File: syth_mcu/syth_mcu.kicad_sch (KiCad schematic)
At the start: 25 parts, among them J1 Conn_01x05, J10 Conn_01x20, J11 Conn_01x20, J2 Conn_01x05, J5 Conn_01x20, J6 Conn_01x20, J7 Conn_01x16, J8 Conn_01x08, SW1 SW_Push, SW2 SW_Push, SW3 SW_Push, SW4 SW_Push, SW5 SW_Push, SW6 SW_Push, SW7 SW_SPST, U2 YAAJ_WeAct_BlackPill_Part_Like, U5 TFT_320x240

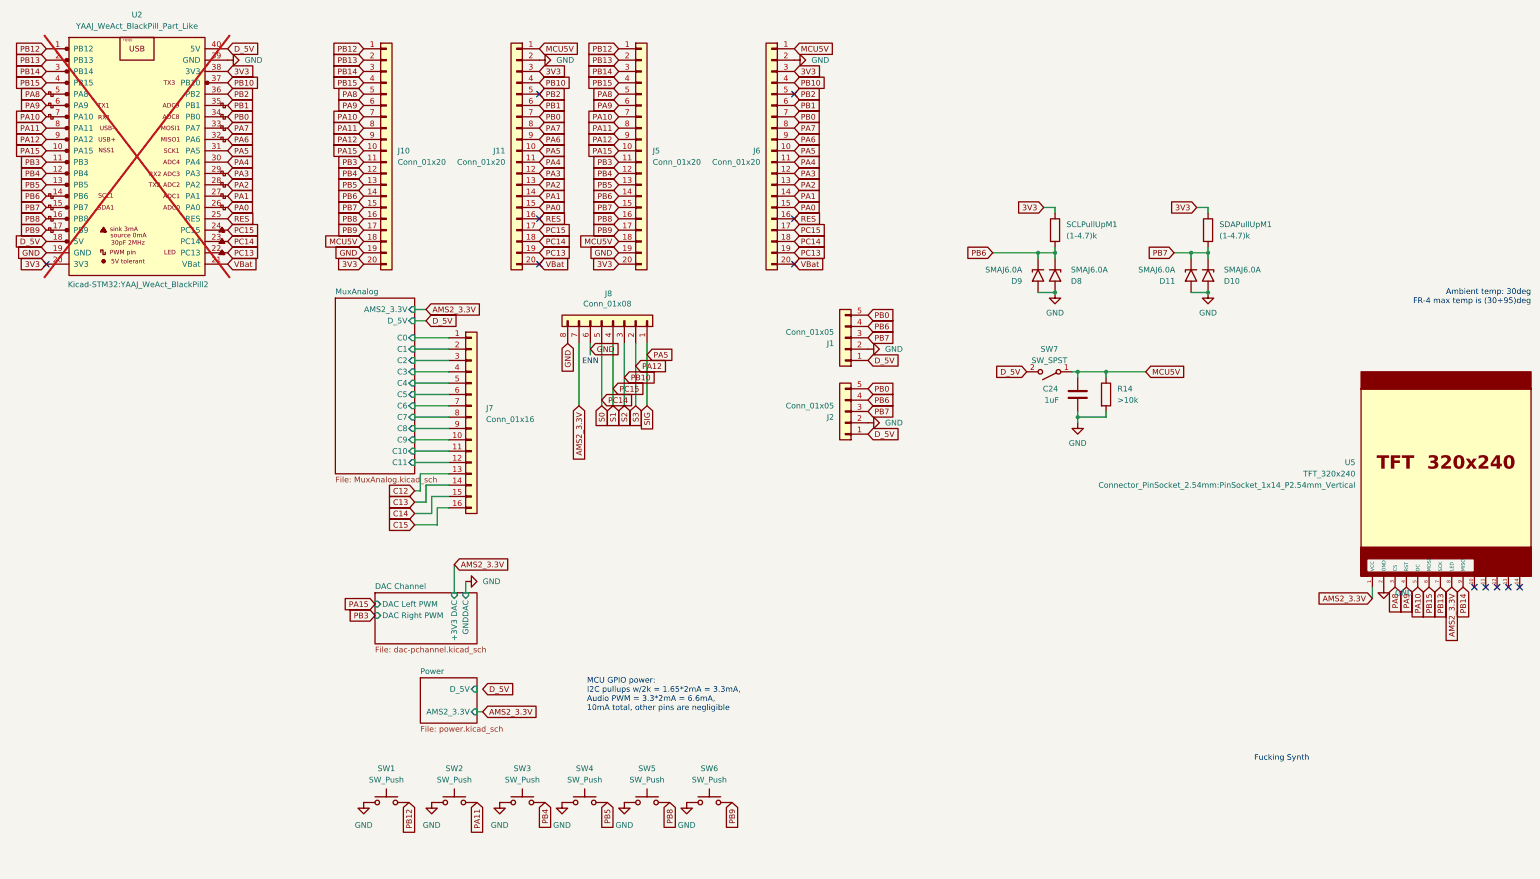
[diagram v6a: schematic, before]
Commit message: v2 schematic merge, power and signal routing
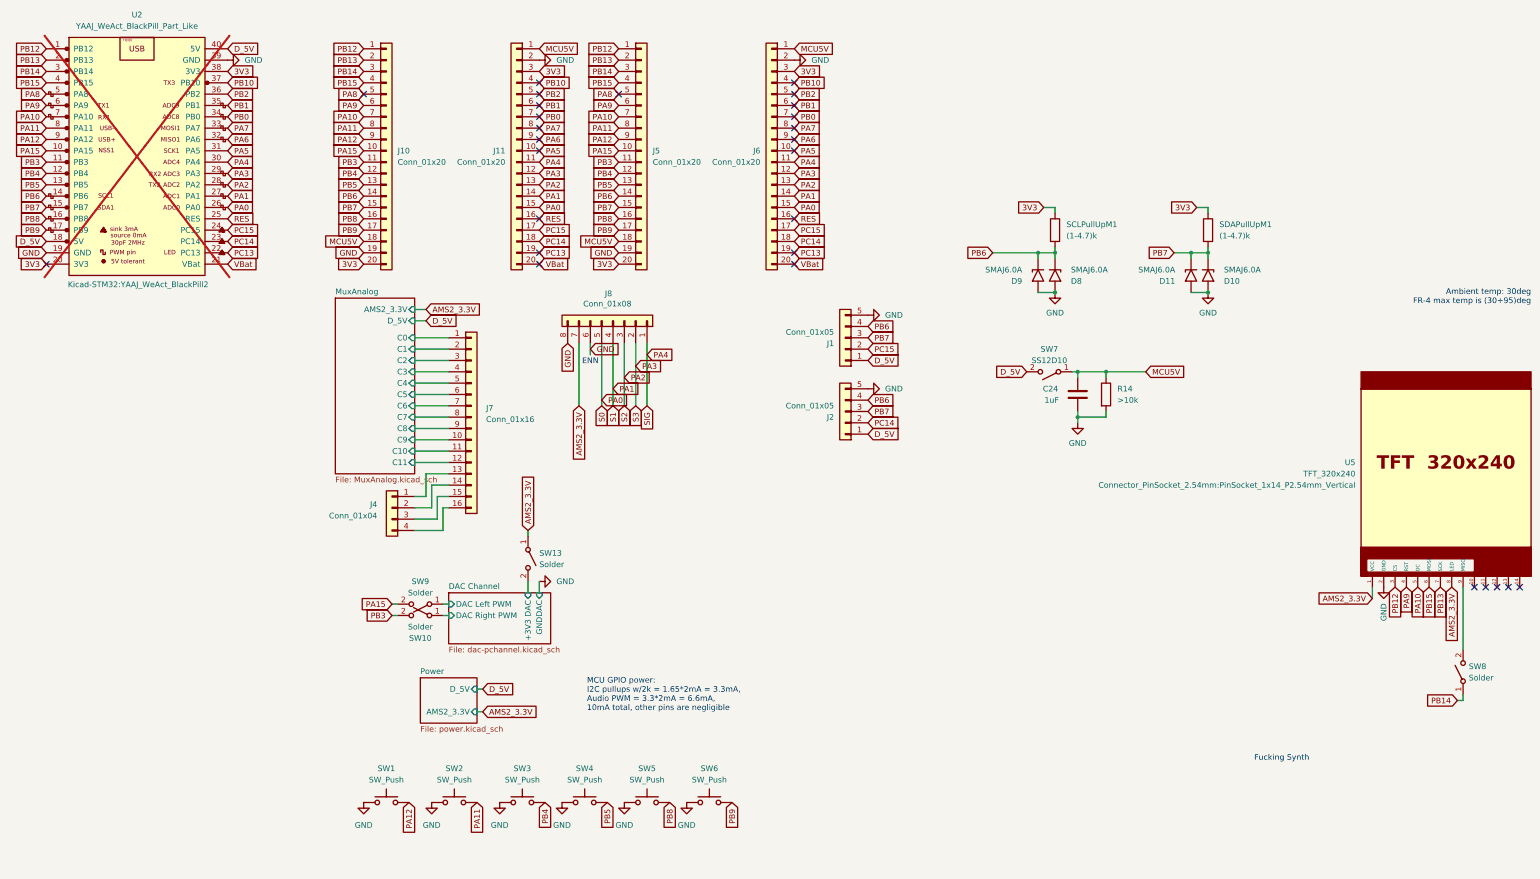
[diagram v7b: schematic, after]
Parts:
- added J4: Conn_01x04, Connector_PinHeader_2.54mm:PinHeader_1x04_P2.54mm_Vertical, symbol Connector_Generic:Conn_01x04
- added SW10, SW13, SW8, SW9: Solder, Jumper:SolderJumper-2_P1.3mm_Open_Pad1.0x1.5mm, symbol Switch:SW_SPST
- SW7: value SW_SPST -> SS12D10
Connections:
- net AMS2_3.3V: now also SW13.1 (A)
- net GND: now also J1.5 (Pin_5), J2.5 (Pin_5); no longer J1.2 (Pin_2), J2.2 (Pin_2)
- net PA0: now also J8.5 (Pin_5)
- net PA1: now also J8.4 (Pin_4)
- net PA12: now also SW1.2; no longer J8.2 (Pin_2)
- net PA15: now also SW9.2 (B)
- net PA2: now also J8.3 (Pin_3)
- net PA3: now also J8.2 (Pin_2)
- net PA4: now also J8.1 (Pin_1)
- net PA5: no longer J8.1 (Pin_1)
- net PA8: no longer U5.3 (CS)
- net PB0: no longer J1.5 (Pin_5), J2.5 (Pin_5)
- net PB10: no longer J8.3 (Pin_3)
- net PB12: now also U5.3 (CS); no longer SW1.2
- net PB14: now also SW8.1 (A); no longer U5.9 (MISO)
- net PB3: now also SW10.2 (B)
- net PC14: now also J2.2 (Pin_2); no longer J8.5 (Pin_5)
- net PC15: now also J1.2 (Pin_2); no longer J8.4 (Pin_4)
- net C12: no longer names the net of J7.13 (Pin_13)
- net C12: now also J4.1 (Pin_1)
- net C13: no longer names the net of J7.14 (Pin_14)
- net C13: now also J4.2 (Pin_2)
- net C14: no longer names the net of J7.15 (Pin_15)
- net C14: now also J4.3 (Pin_3)
- net C15: no longer names the net of J7.16 (Pin_16)
- net C15: now also J4.4 (Pin_4)
- new net: SW8.2 (B), U5.9 (MISO)
- new net DAC Channel/+3V3 DAC: SW13.2 (B)
- new net DAC Channel/DAC Left PWM: SW9.1 (A)
- new net DAC Channel/DAC Right PWM: SW10.1 (A)
- no-connect marks 12 -> 28

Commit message: Added DIP switch, mux and switch switched places, SPI CS now PA8
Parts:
- removed J1, J2: Conn_01x05, synth:CONN-TH_PR5L4015-5P-C-F, symbol Connector_Generic:Conn_01x05
- added LeftConn1: Conn_01x08, Connector_PinSocket_2.54mm:PinSocket_1x08_P2.54mm_Horizontal, symbol Connector_Generic:Conn_01x08
- added RightConn1: Conn_01x08, Connector_PinHeader_2.54mm:PinHeader_1x08_P2.54mm_Horizontal, symbol Connector_Generic:Conn_01x08
- added SW11: SW_DIP_x03, synth:DIPSwitch3, symbol Switch:SW_DIP_x03
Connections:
- net D_5V: now also LeftConn1.4 (Pin_4), RightConn1.4 (Pin_4)
- net GND: now also LeftConn1.8 (Pin_8), RightConn1.8 (Pin_8), SW11.4, SW11.5, SW11.6
- net PA8: now also U5.3 (CS)
- net PB0: now also SW11.3
- net PB1: now also SW11.2
- net PB10: now also SW11.1
- net PB12: no longer U5.3 (CS)
- net PB6: now also LeftConn1.7 (Pin_7), RightConn1.7 (Pin_7)
- net PB7: now also LeftConn1.6 (Pin_6), RightConn1.6 (Pin_6)
- net PC14: now also RightConn1.5 (Pin_5)
- net PC15: now also LeftConn1.5 (Pin_5)
